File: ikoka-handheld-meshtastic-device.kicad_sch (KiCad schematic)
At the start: 41 parts, among them J1 Conn_Coaxial, J4 1.25-2PWB, Q1 AO3401A, SW1 SW_Push, SW2 SW_Push, U1 MT3608B, U2 E22-900M30S, U3 XIAO-nRF52840-SMD, U4 TP4056-42-ESOP8

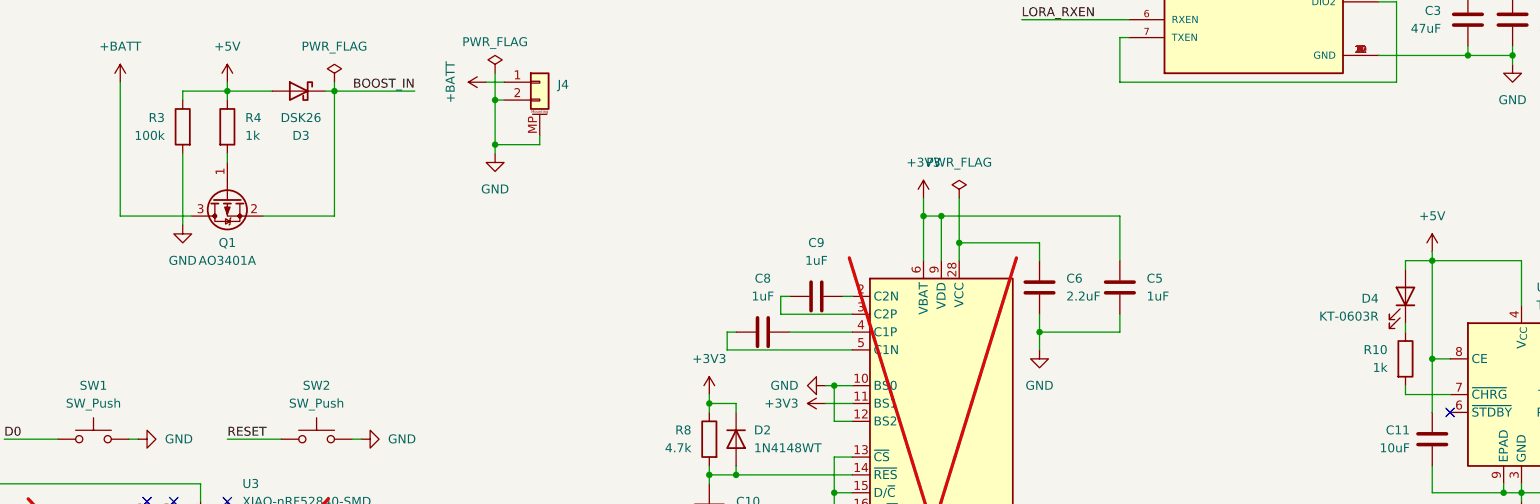
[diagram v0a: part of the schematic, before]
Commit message: feat: Use more 1.5k and 300k resistors where possible to simplify BoM
Signed-off-by: Andrew Yong <me@ndoo.sg>
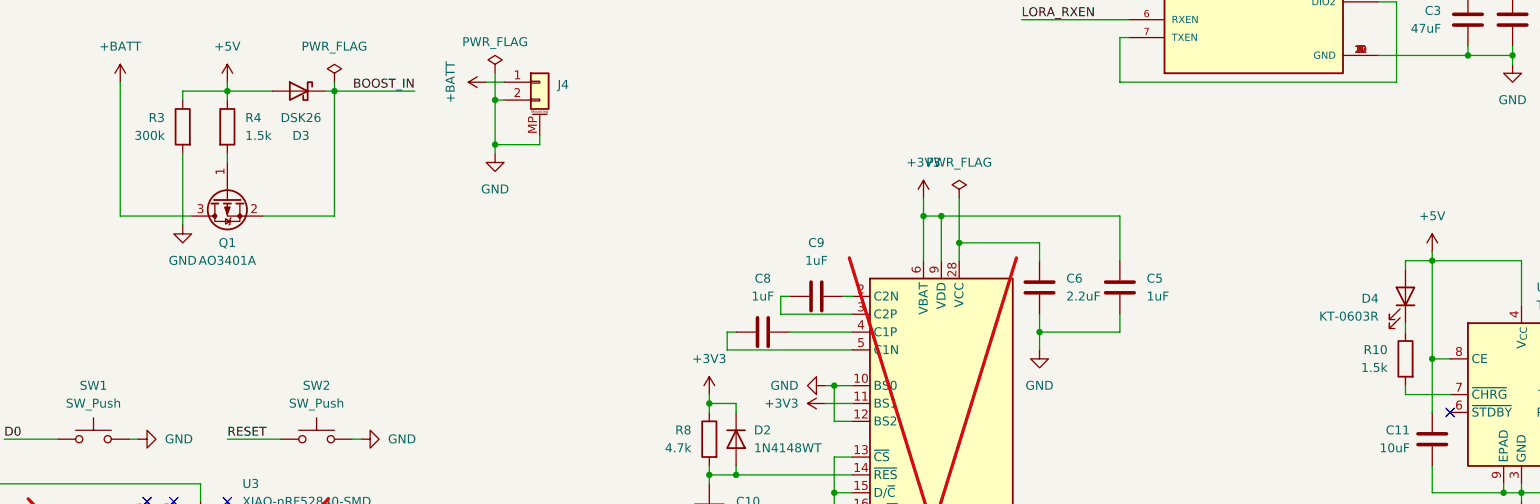
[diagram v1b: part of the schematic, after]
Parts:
- R10, R4: value 1k -> 1.5k
- R3: value 100k -> 300k
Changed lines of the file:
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@@
 		(lib_id "Device:R")
 		(at 224.79 121.92 0)
+		(mirror y)
 		(unit 1)
 		(exclude_from_sim no)
@@
 					(size 1.27 1.27)
 				)
-				(justify right)
+				(justify left)
 			)
 		)
-		(property "Value" "1k"
+		(property "Value" "1.5k"
 			(at 222.25 123.1899 0)
 			(effects
@@
 					(size 1.27 1.27)
 				)
-				(justify right)
+				(justify left)
 			)
 		)
 		(property "Footprint" "Resistor_SMD:R_0603_1608Metric"
-			(at 223.012 121.92 90)
+			(at 226.568 121.92 90)
 			(effects
 				(font
@@
 		)
 		(property "LCSC" "C23024"
-			(at 227.33 120.6499 0)
+			(at 222.25 120.6499 0)
 			(effects
 				(font
@@
 			)
 		)
-		(property "Value" "100k"
+		(property "Value" "300k"
 			(at 48.26 90.1699 0)
 			(effects
@@
 			)
 		)
-		(property "Value" "1k"
+		(property "Value" "1.5k"
 			(at 59.69 90.1699 0)
 			(effects

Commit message: feat: OSHW logo
Signed-off-by: Andrew Yong <me@ndoo.sg>
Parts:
- added SYM1: Logo_Open_Hardware_Small, Symbol:OSHW-Logo_19x20mm_SilkScreen, symbol Graphic:Logo_Open_Hardware_Small
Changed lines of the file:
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@@
+	)
+	(symbol
+		(lib_id "Graphic:Logo_Open_Hardware_Small")
+		(at 273.05 158.75 0)
+		(unit 1)
+		(exclude_from_sim no)
+		(in_bom no)
+		(on_board yes)
+		(dnp no)
+		(fields_autoplaced yes)
+		(property "Reference" "SYM1"
+			(at 273.05 151.765 0)
+			(effects
+				(font
+					(size 1.27 1.27)
+				)
+				(hide yes)
+			)
+		)
+		(property "Value" "Logo_Open_Hardware_Small"
+			(at 273.05 164.465 0)
+			(effects
+				(font
+					(size 1.27 1.27)
+				)
+				(hide yes)
+			)
+		)
+		(property "Footprint" "Symbol:OSHW-Logo_19x20mm_SilkScreen"
+			(at 273.05 158.75 0)
+			(effects
+				(font
+					(size 1.27 1.27)
+				)
+				(hide yes)
+			)
+		)
+		(property "Datasheet" "~"
+			(at 273.05 158.75 0)
+			(effects
+				(font
+					(size 1.27 1.27)
+				)
+				(hide yes)
+			)
+		)
+		(property "Description" "Open Hardware logo, small"
+			(at 273.05 158.75 0)
+			(effects
+				(font
+					(size 1.27 1.27)
+				)
+				(hide yes)
+			)
+		)
+		(property "Sim.Enable" "0"
+			(at 273.05 158.75 0)
+			(effects
+				(font
+					(size 1.27 1.27)
+				)
+				(hide yes)
+			)
+		)
+		(instances
+			(project ""
+				(path "/d817f34c-2aa5-4c70-878b-29719eb987fe"
+					(reference "SYM1")
+					(unit 1)
+				)
+			)
+		)
 	)
 	(symbol

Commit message: fixup! fix: Change inductor from 22uH to 2.2uH, Move XIAO up 0.1mm
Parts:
- C10, C7: LCSC C59461 -> C19666
- C11, C12: LCSC C59461 -> C19702
- C5, C8, C9: LCSC C59461 -> C15849
- C6: LCSC C59461 -> C23630
- D1, D3: LCSC C8678 -> C7502712
- D2: LCSC (none) -> C7420320
- D4: LCSC (none) -> C2286
- L1: LCSC C18724424 -> C167747
- Q1: LCSC (none) -> C15127
- R10, R4, R9: LCSC C23024 -> C22843
- R6, R7, R8: LCSC C23024 -> C23162
- SW1, SW2: LCSC C318884 -> C720477
- U1: LCSC C2932326 -> C19189893
- U4: LCSC (none) -> C16581
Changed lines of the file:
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@@
 			)
 		)
-		(property "LCSC" "C8678"
+		(property "LCSC" "C7502712"
 			(at 67.6275 90.17 0)
 			(effects
@@
 			)
 		)
+		(property "LCSC" "C15127"
+			(at 57.15 105.41 0)
+			(effects
+				(font
+					(size 1.27 1.27)
+				)
+				(hide yes)
+			)
+		)
 		(pin "3"
 		)
@@
 			)
 		)
-		(property "LCSC" "C59461"
+		(property "LCSC" "C19702"
 			(at 269.24 133.3499 0)
 			(effects
@@
 			)
 		)
-		(property "LCSC" "C59461"
+		(property "LCSC" "C15849"
 			(at 139.6999 109.22 0)
 			(effects
@@
 			)
 		)
-		(property "LCSC" "C23024"
+		(property "LCSC" "C22843"
 			(at 222.25 120.6499 0)
 			(effects
@@
 			)
 		)
-		(property "LCSC" "C59461"
+		(property "LCSC" "C19666"
 			(at 147.32 180.3399 0)
 			(effects
@@
 			)
 		)
-		(property "LCSC" "C59461"
+		(property "LCSC" "C19702"
 			(at 224.79 132.0799 0)
 			(effects
@@
 			)
 		)
-		(property "LCSC" "C59461"
+		(property "LCSC" "C23630"
 			(at 176.53 110.4899 0)
 			(effects
@@
 			)
 		)
-		(property "LCSC" "C18724424"
+		(property "LCSC" "C167747"
 			(at 45.72 20.32 0)
 			(effects
@@
 			)
 		)
-		(property "LCSC" "C318884"
+		(property "LCSC" "C720477"
 			(at 69.85 125.73 0)
 			(effects
@@
 			)
 		)
+		(property "LCSC" "C2286"
+			(at 220.98 113.3474 0)
+			(effects
+				(font
+					(size 1.27 1.27)
+				)
+				(hide yes)
+			)
+		)
 		(pin "2"
 		)
@@
 			)
 		)
-		(property "LCSC" "C23024"
+		(property "LCSC" "C23162"
 			(at 123.19 132.0799 0)
 			(effects
@@
 			)
 		)
-		(property "LCSC" "C59461"
+		(property "LCSC" "C19666"
 			(at 129.54 142.2399 0)
 			(effects
@@
 			)
 		)
-		(property "LCSC" "C23024"
+		(property "LCSC" "C23162"
 			(at 139.7 160.0199 0)
 			(effects
@@
 			)
 		)
-		(property "LCSC" "C23024"
+		(property "LCSC" "C22843"
 			(at 252.73 133.3499 0)
 			(effects
@@
 			)
 		)
-		(property "LCSC" "C8678"
+		(property "LCSC" "C7502712"
 			(at 60.0075 19.05 0)
 			(effects
@@
 			)
 		)
-		(property "LCSC" "C59461"
+		(property "LCSC" "C15849"
 			(at 132.0799 114.3 0)
 			(effects
@@
 			)
 		)
-		(property "LCSC" "C59461"
+		(property "LCSC" "C15849"
 			(at 187.96 110.4899 0)
 			(effects
@@
 			)
 		)
-		(property "LCSC" "C23024"
+		(property "LCSC" "C23162"
 			(at 130.81 160.0199 0)
 			(effects
@@
 			)
 		)
-		(property "LCSC" "C2932326"
+		(property "LCSC" "C19189893"
 			(at 45.72 27.94 0)
 			(effects
@@
 			)
 		)
+		(property "LCSC" "C16581"
+			(at 243.4433 111.76 0)
+			(effects
+				(font
+					(size 1.27 1.27)
+				)
+				(hide yes)
+			)
+		)
 		(pin "5"
 		)
@@
 			)
 		)
+		(property "LCSC" "C7420320"
+			(at 132.08 132.0799 0)
+			(effects
+				(font
+					(size 1.27 1.27)
+				)
+				(hide yes)
+			)
+		)
 		(pin "1"
 		)
@@
 			)
 		)
-		(property "LCSC" "C318884"
+		(property "LCSC" "C720477"
 			(at 38.1 125.73 0)
 			(effects
@@
 			)
 		)
-		(property "LCSC" "C23024"
+		(property "LCSC" "C22843"
 			(at 59.69 87.6299 0)
 			(effects

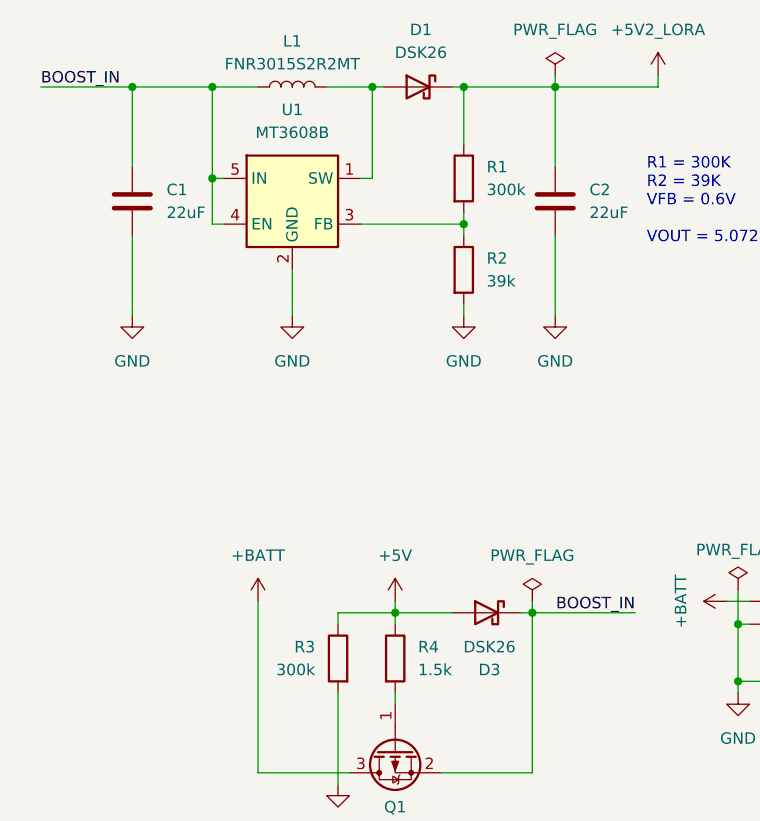
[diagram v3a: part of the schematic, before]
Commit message: feat: Boost converter improvements
- Change Schottky diode from DSK26 (Vf 0.7V, Iav 2A) to DSK34 (Vf 0.55V, Iav 3A)
- Change inductor from FNR3015S2R2MT (2.2µH, 2A/2A, DCR 0.06Ω) to FTC303018D4R7MBCA (4.7µH, 4.2A/3A, DCR 0.087Ω)

Signed-off-by: Andrew Yong <me@ndoo.sg>
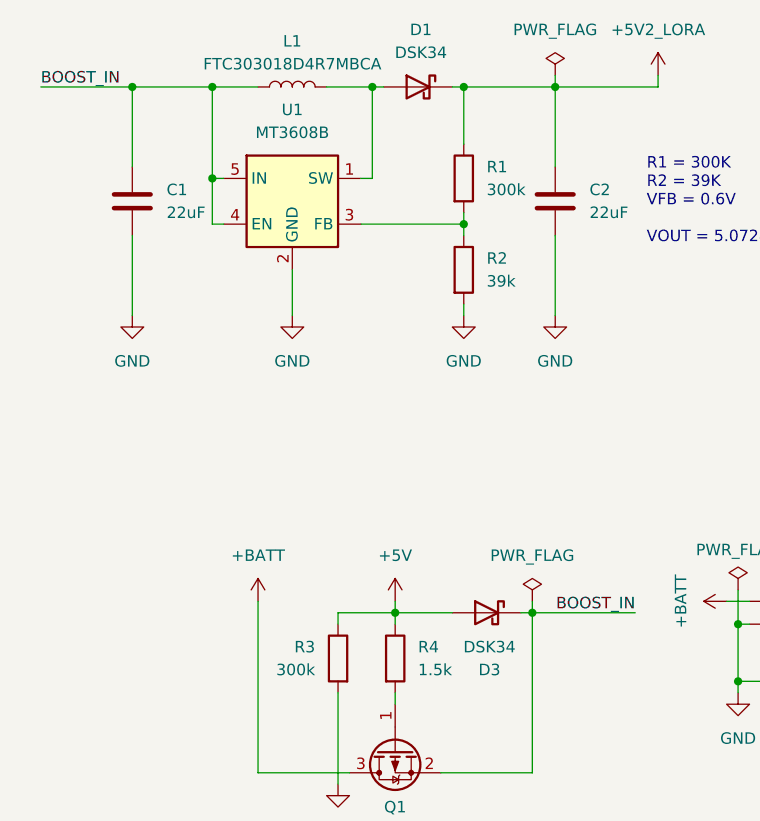
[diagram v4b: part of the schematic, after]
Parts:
- D1, D3: value DSK26 -> DSK34; LCSC C7502712 -> C22466353
- L1: value FNR3015S2R2MT -> FTC303018D4R7MBCA; footprint Inductor_SMD:L_Changjiang_FNR3015S -> Inductor_SMD:L_Changjiang_FTC303018D
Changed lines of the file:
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@@
 			)
 		)
-		(property "Value" "DSK26"
+		(property "Value" "DSK34"
 			(at 67.6275 87.63 0)
 			(effects
@@
 			)
 		)
-		(property "LCSC" "C7502712"
+		(property "LCSC" "C22466353"
 			(at 67.6275 90.17 0)
 			(effects
@@
 			)
 		)
-		(property "Value" "FNR3015S2R2MT"
+		(property "Value" "FTC303018D4R7MBCA"
 			(at 45.72 22.86 90)
 			(effects
@@
 			)
 		)
-		(property "Footprint" "Inductor_SMD:L_Changjiang_FNR3015S"
+		(property "Footprint" "Inductor_SMD:L_Changjiang_FTC303018D"
 			(at 45.72 25.4 0)
 			(effects
@@
 		(at 273.05 158.75 0)
 		(unit 1)
-		(exclude_from_sim no)
+		(exclude_from_sim yes)
 		(in_bom no)
 		(on_board yes)
@@
 			)
 		)
-		(property "Sim.Enable" "0"
-			(at 273.05 158.75 0)
-			(effects
-				(font
-					(size 1.27 1.27)
-				)
-				(hide yes)
-			)
-		)
 		(instances
 			(project ""
@@
 			)
 		)
-		(property "Value" "DSK26"
+		(property "Value" "DSK34"
 			(at 60.0075 21.59 0)
 			(effects
@@
 			)
 		)
-		(property "LCSC" "C7502712"
+		(property "LCSC" "C22466353"
 			(at 60.0075 19.05 0)
 			(effects

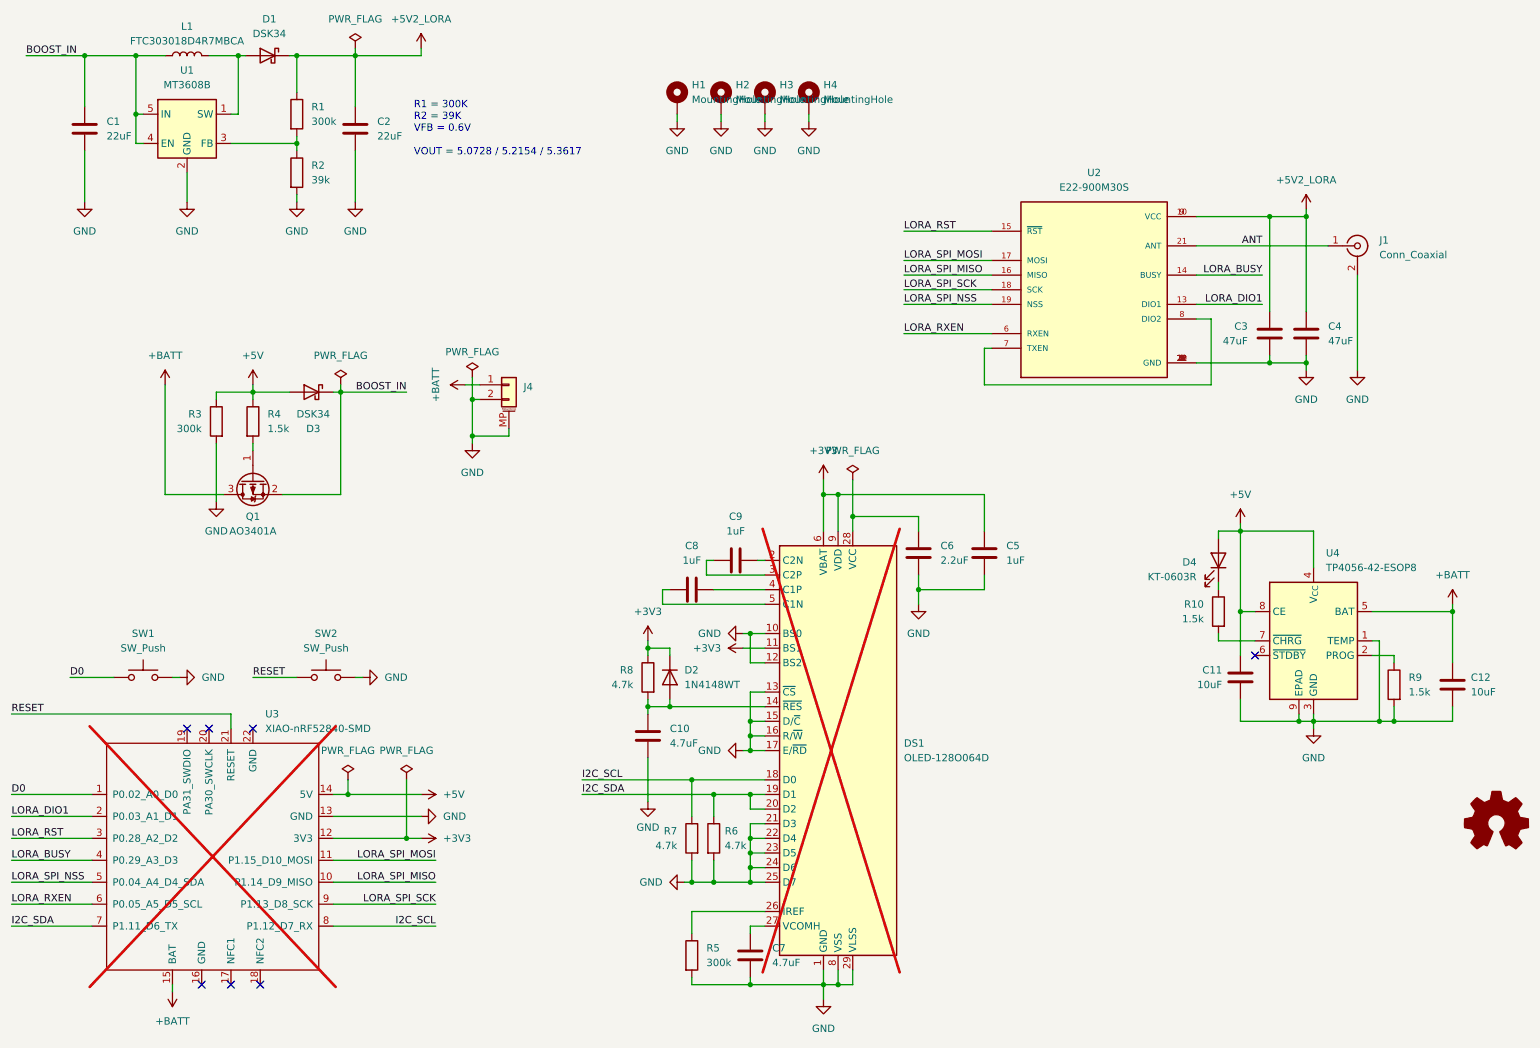
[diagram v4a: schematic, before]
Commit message: fix: Remove I2C 4.7kΩ pull-down resistors - The resistors are wrongly wired as pull-down to GND instead of pull-up to 3V3, I2C is open drain and requires pull-up - Remove them entirely and rely on nrf52840 internal 13kΩ pull-up for I2C, this is sufficient for SSD1306 I2C speeds - Future addition of I2C external connector should provision pull-ups for stability
Fixes #3.

Signed-off-by: Andrew Yong <me@ndoo.sg>
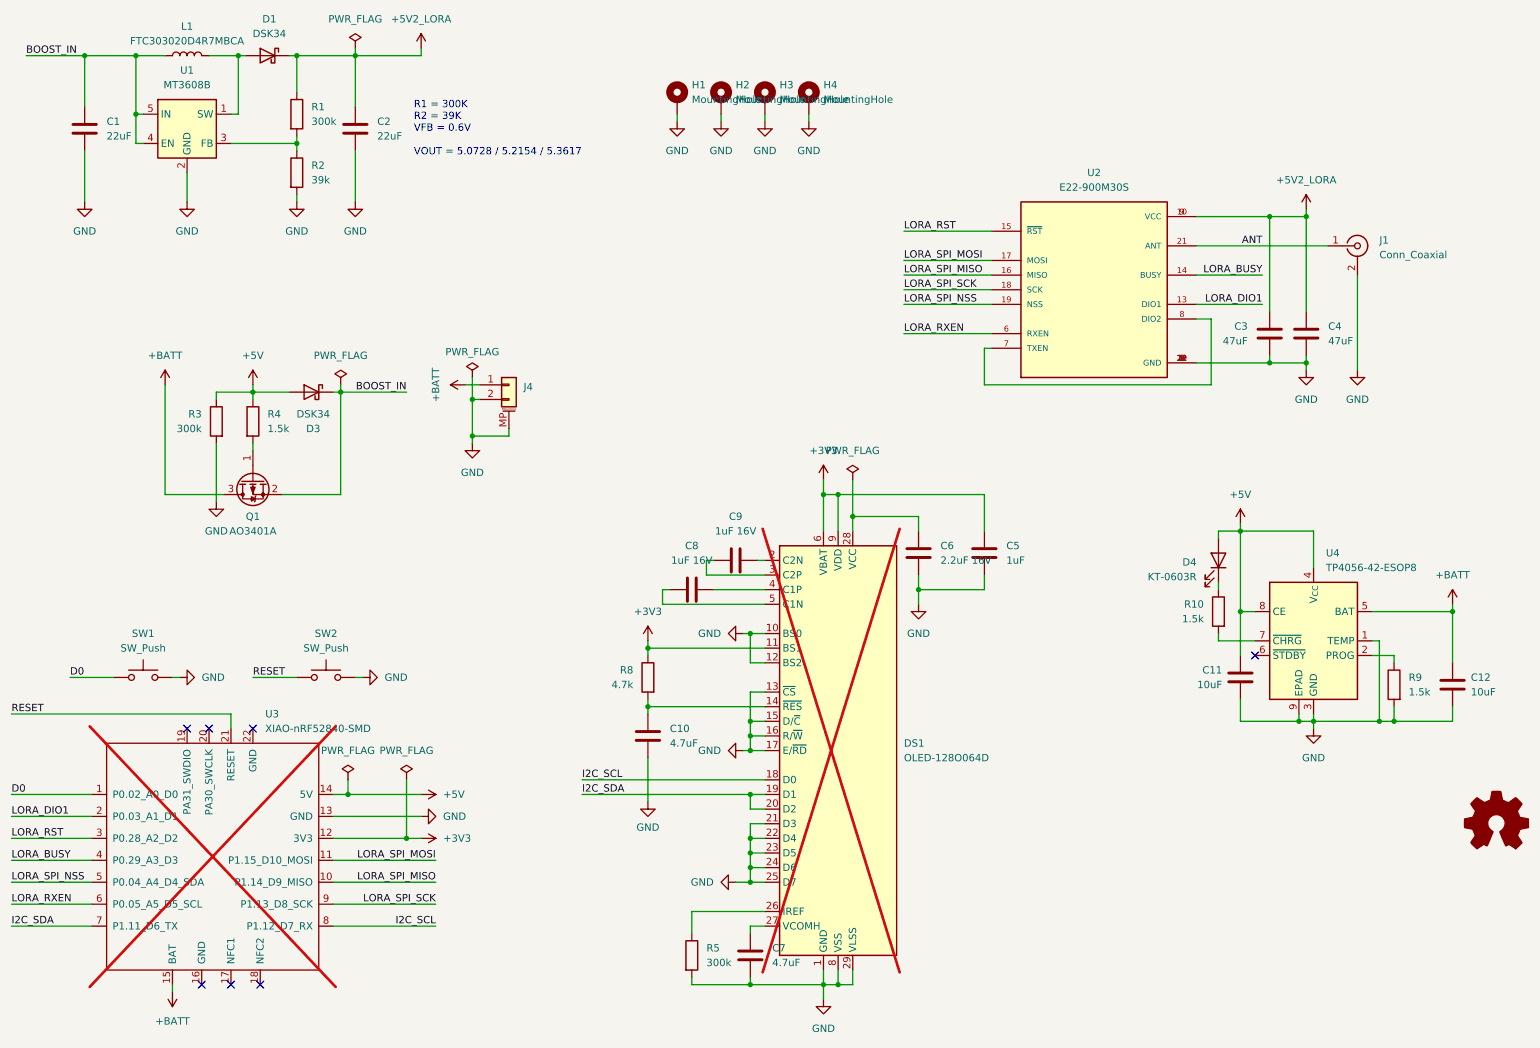
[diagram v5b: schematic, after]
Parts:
- removed D2: 1N4148WT, Diode_SMD:D_SOD-523, symbol Device:D
- removed R6, R7: 4.7k, Resistor_SMD:R_0603_1608Metric, symbol Device:R
- C6: value 2.2uF -> 2.2uF 16V
- C8, C9: value 1uF -> 1uF 16V
- L1: value FTC303018D4R7MBCA -> FTC303020D4R7MBCA; footprint Inductor_SMD:L_Changjiang_FTC303018D -> Inductor_SMD:L_Changjiang_FTC303020D
- SYM1: footprint Symbol:OSHW-Logo_19x20mm_SilkScreen -> Symbol:OSHW-Logo_7.5x8mm_SilkScreen
